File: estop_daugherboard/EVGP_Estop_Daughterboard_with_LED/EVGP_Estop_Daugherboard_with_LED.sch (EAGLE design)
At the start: 46 parts, among them J1 STEERING, J2 DRIVE, J3 JST-XH-03-PIN-LONG-PAD, J4 JST-XH-03-PIN-LONG-PAD, J5 AVR_SPI_PROG_3X2PTH, J6 UX60-MB-5S8, J7 JST-XH-04-PACKAGE-LONG-PAD, Q1 N_FET2, Q2 N_FET1, U1 LM555CMX/NOPBM08A-M, U2 NL27WZ08USG, U3 ATMEGA32U4-AU, X1 TSX-3225 16.0000MF18X-AC0

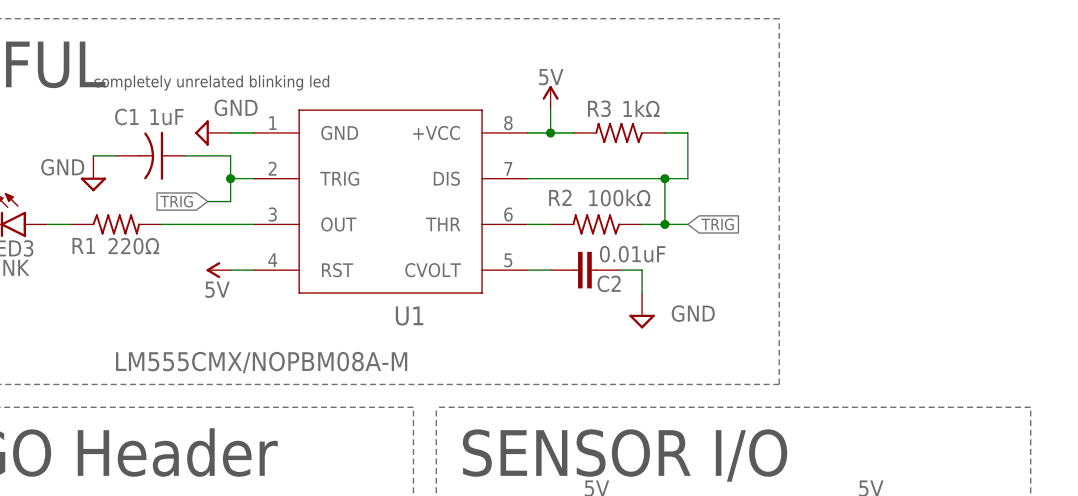
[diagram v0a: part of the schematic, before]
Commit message: Changed the library name, added 555 to library, implemented into both 'normal' and 'led' boards
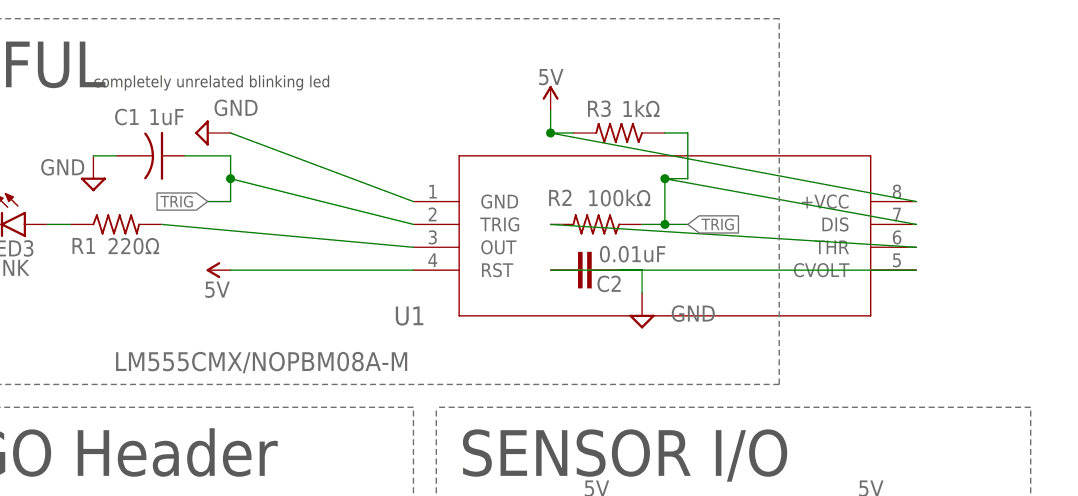
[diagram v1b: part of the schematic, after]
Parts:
- J1, J2: device Rembrandt Electronics - JST XH Connectors v1-0:JST-XH-02-PIN-LONG-PAD -> EVGP_Estop_Daughterboard:JST-XH-02-PIN-LONG-PAD
- J3, J4: device Rembrandt Electronics - JST XH Connectors v1-0:JST-XH-03-PIN-LONG-PAD -> EVGP_Estop_Daughterboard:JST-XH-03-PIN-LONG-PAD
- J7: device Rembrandt Electronics - JST XH Connectors v1-0:JST-XH-04-PIN-LONG-PAD -> EVGP_Estop_Daughterboard:JST-XH-04-PIN-LONG-PAD
- Q1, Q2: device Daughterboard-Stuff:BSS84DW-7-F -> EVGP_Estop_Daughterboard:BSS84DW-7-F
- U1: device 555:LM555CMX/NOPBM08A-M -> EVGP_Estop_Daughterboard:LM555CMX/NOPBM08A-M
- U2: device Daughterboard-Stuff:NL27WZ08USG -> EVGP_Estop_Daughterboard:NL27WZ08USG
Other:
- moved on the sheet: U1
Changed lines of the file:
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@@
 <part name="GND2" library="SparkFun-PowerSymbols" deviceset="GND" device=""/>
 <part name="SUPPLY8" library="SparkFun-PowerSymbols" deviceset="5V" device=""/>
-<part name="U2" library="Daughterboard-Stuff" deviceset="NL27WZ08USG" device=""/>
+<part name="U2" library="EVGP_Estop_Daughterboard" deviceset="NL27WZ08USG" device=""/>
 <part name="SUPPLY9" library="SparkFun-PowerSymbols" deviceset="5V" device=""/>
 <part name="GND3" library="SparkFun-PowerSymbols" deviceset="GND" device=""/>
 <part name="R11" library="rcl" library_urn="urn:adsk.eagle:library:334" deviceset="R-US_" device="R0603" package3d_urn="urn:adsk.eagle:package:23555/3" value="10kΩ"/>
-<part name="Q2" library="Daughterboard-Stuff" deviceset="BSS84DW-7-F" device="" value="N_FET1"/>
-<part name="Q1" library="Daughterboard-Stuff" deviceset="BSS84DW-7-F" device="" value="N_FET2"/>
+<part name="Q2" library="EVGP_Estop_Daughterboard" deviceset="BSS84DW-7-F" device="" value="N_FET1"/>
+<part name="Q1" library="EVGP_Estop_Daughterboard" deviceset="BSS84DW-7-F" device="" value="N_FET2"/>
 <part name="P+3" library="supply1" library_urn="urn:adsk.eagle:library:371" deviceset="+24V" device=""/>
 <part name="SUPPLY22" library="supply2" library_urn="urn:adsk.eagle:library:372" deviceset="GND" device=""/>
@@
 <part name="SUPPLY30" library="supply2" library_urn="urn:adsk.eagle:library:372" deviceset="GND" device=""/>
 <part name="SUPPLY31" library="supply2" library_urn="urn:adsk.eagle:library:372" deviceset="GND" device=""/>
-<part name="J7" library="Rembrandt Electronics - JST XH Connectors v1-0" deviceset="JST-XH-04-PIN" device="-LONG-PAD" value="JST-XH-04-PACKAGE-LONG-PAD"/>
-<part name="J2" library="Rembrandt Electronics - JST XH Connectors v1-0" deviceset="JST-XH-02-PIN" device="-LONG-PAD" value="DRIVE"/>
-<part name="J1" library="Rembrandt Electronics - JST XH Connectors v1-0" deviceset="JST-XH-02-PIN" device="-LONG-PAD" value="STEERING"/>
-<part name="J4" library="Rembrandt Electronics - JST XH Connectors v1-0" deviceset="JST-XH-03-PIN" device="-LONG-PAD"/>
+<part name="J7" library="EVGP_Estop_Daughterboard" deviceset="JST-XH-04-PIN" device="-LONG-PAD" value="JST-XH-04-PACKAGE-LONG-PAD"/>
+<part name="J2" library="EVGP_Estop_Daughterboard" deviceset="JST-XH-02-PIN" device="-LONG-PAD" value="DRIVE"/>
+<part name="J1" library="EVGP_Estop_Daughterboard" deviceset="JST-XH-02-PIN" device="-LONG-PAD" value="STEERING"/>
+<part name="J4" library="EVGP_Estop_Daughterboard" deviceset="JST-XH-03-PIN" device="-LONG-PAD"/>
 <part name="GND5" library="SparkFun-PowerSymbols" deviceset="GND" device=""/>
 <part name="GND9" library="SparkFun-PowerSymbols" deviceset="GND" device=""/>
 <part name="GND12" library="SparkFun-PowerSymbols" deviceset="GND" device=""/>
 <part name="SUPPLY10" library="SparkFun-PowerSymbols" deviceset="5V" device=""/>
-<part name="J3" library="Rembrandt Electronics - JST XH Connectors v1-0" deviceset="JST-XH-03-PIN" device="-LONG-PAD"/>
+<part name="J3" library="EVGP_Estop_Daughterboard" deviceset="JST-XH-03-PIN" device="-LONG-PAD"/>
 <part name="GND13" library="SparkFun-PowerSymbols" deviceset="GND" device=""/>
 <part name="SUPPLY11" library="SparkFun-PowerSymbols" deviceset="5V" device=""/>
@@
 <attribute name="SCH_DESC" value="EVGP Steering Control Board "/>
 </part>
-<part name="U1" library="555" deviceset="LM555CMX/NOPB" device="M08A-M"/>
+<part name="U1" library="EVGP_Estop_Daughterboard" deviceset="LM555CMX/NOPB" device="M08A-M"/>
 <part name="SUPPLY7" library="supply2" library_urn="urn:adsk.eagle:library:372" deviceset="GND" device=""/>
 <part name="SUPPLY12" library="SparkFun-PowerSymbols" deviceset="5V" device=""/>
@@
 <pinref part="SUPPLY7" gate="GND" pin="GND"/>
 <pinref part="U1" gate="A" pin="GND"/>
-<wire x1="210.82" y1="213.36" x2="208.28" y2="213.36" width="0.1524" layer="91"/>
+<wire x1="228.6" y1="205.74" x2="208.28" y2="213.36" width="0.1524" layer="91"/>
 </segment>
 <segment>
@@
 <segment>
 <pinref part="SUPPLY15" gate="G$1" pin="5V"/>
-<wire x1="208.28" y1="198.12" x2="210.82" y2="198.12" width="0.1524" layer="91"/>
+<wire x1="208.28" y1="198.12" x2="228.6" y2="198.12" width="0.1524" layer="91"/>
 <pinref part="U1" gate="A" pin="RST"/>
 </segment>
 <segment>
 <pinref part="U1" gate="A" pin="+VCC"/>
-<wire x1="241.3" y1="213.36" x2="243.84" y2="213.36" width="0.1524" layer="91"/>
+<wire x1="284.48" y1="205.74" x2="243.84" y2="213.36" width="0.1524" layer="91"/>
 <pinref part="R3" gate="G$1" pin="2"/>
 <wire x1="246.38" y1="213.36" x2="243.84" y2="213.36" width="0.1524" layer="91"/>
@@
 <pinref part="R2" gate="G$1" pin="2"/>
 <pinref part="U1" gate="A" pin="THR"/>
-<wire x1="243.84" y1="203.2" x2="241.3" y2="203.2" width="0.1524" layer="91"/>
+<wire x1="243.84" y1="203.2" x2="284.48" y2="200.66" width="0.1524" layer="91"/>
 </segment>
 </net>
@@
 <pinref part="C2" gate="G$1" pin="1"/>
 <pinref part="U1" gate="A" pin="CVOLT"/>
-<wire x1="243.84" y1="198.12" x2="241.3" y2="198.12" width="0.1524" layer="91"/>
+<wire x1="243.84" y1="198.12" x2="284.48" y2="198.12" width="0.1524" layer="91"/>
 </segment>
 </net>
@@
 <segment>
 <pinref part="U1" gate="A" pin="TRIG"/>
-<wire x1="210.82" y1="208.28" x2="208.28" y2="208.28" width="0.1524" layer="91"/>
+<wire x1="228.6" y1="203.2" x2="208.28" y2="208.28" width="0.1524" layer="91"/>
 <wire x1="208.28" y1="208.28" x2="208.28" y2="205.74" width="0.1524" layer="91"/>
 <wire x1="208.28" y1="205.74" x2="205.74" y2="205.74" width="0.1524" layer="91"/>
@@
 <wire x1="259.08" y1="213.36" x2="259.08" y2="208.28" width="0.1524" layer="91"/>
 <pinref part="U1" gate="A" pin="DIS"/>
-<wire x1="241.3" y1="208.28" x2="256.54" y2="208.28" width="0.1524" layer="91"/>
+<wire x1="284.48" y1="203.2" x2="256.54" y2="208.28" width="0.1524" layer="91"/>
 <pinref part="R2" gate="G$1" pin="1"/>
 <wire x1="256.54" y1="208.28" x2="259.08" y2="208.28" width="0.1524" layer="91"/>
@@
 <pinref part="U1" gate="A" pin="OUT"/>
 <pinref part="R1" gate="G$1" pin="2"/>
-<wire x1="200.66" y1="203.2" x2="210.82" y2="203.2" width="0.1524" layer="91"/>
-</segment>
-</net>
+<wire x1="200.66" y1="203.2" x2="228.6" y2="200.66" width="0.1524" layer="91"/>
+</segment>
+</net>
